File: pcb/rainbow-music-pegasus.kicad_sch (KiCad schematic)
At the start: 111 parts, among them J1 USB_B_Micro, J2 Conn_02x03_Odd_Even, J3 B2B-PH-K-S, Q1 DMG3415U, SW1 SW_SPDT, SW2 EVQQ2, U1 ESP32-C3-MINI-1, U2 OPA2322, U3 TLV75533PDBV, U4 MCP73831-2-OT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

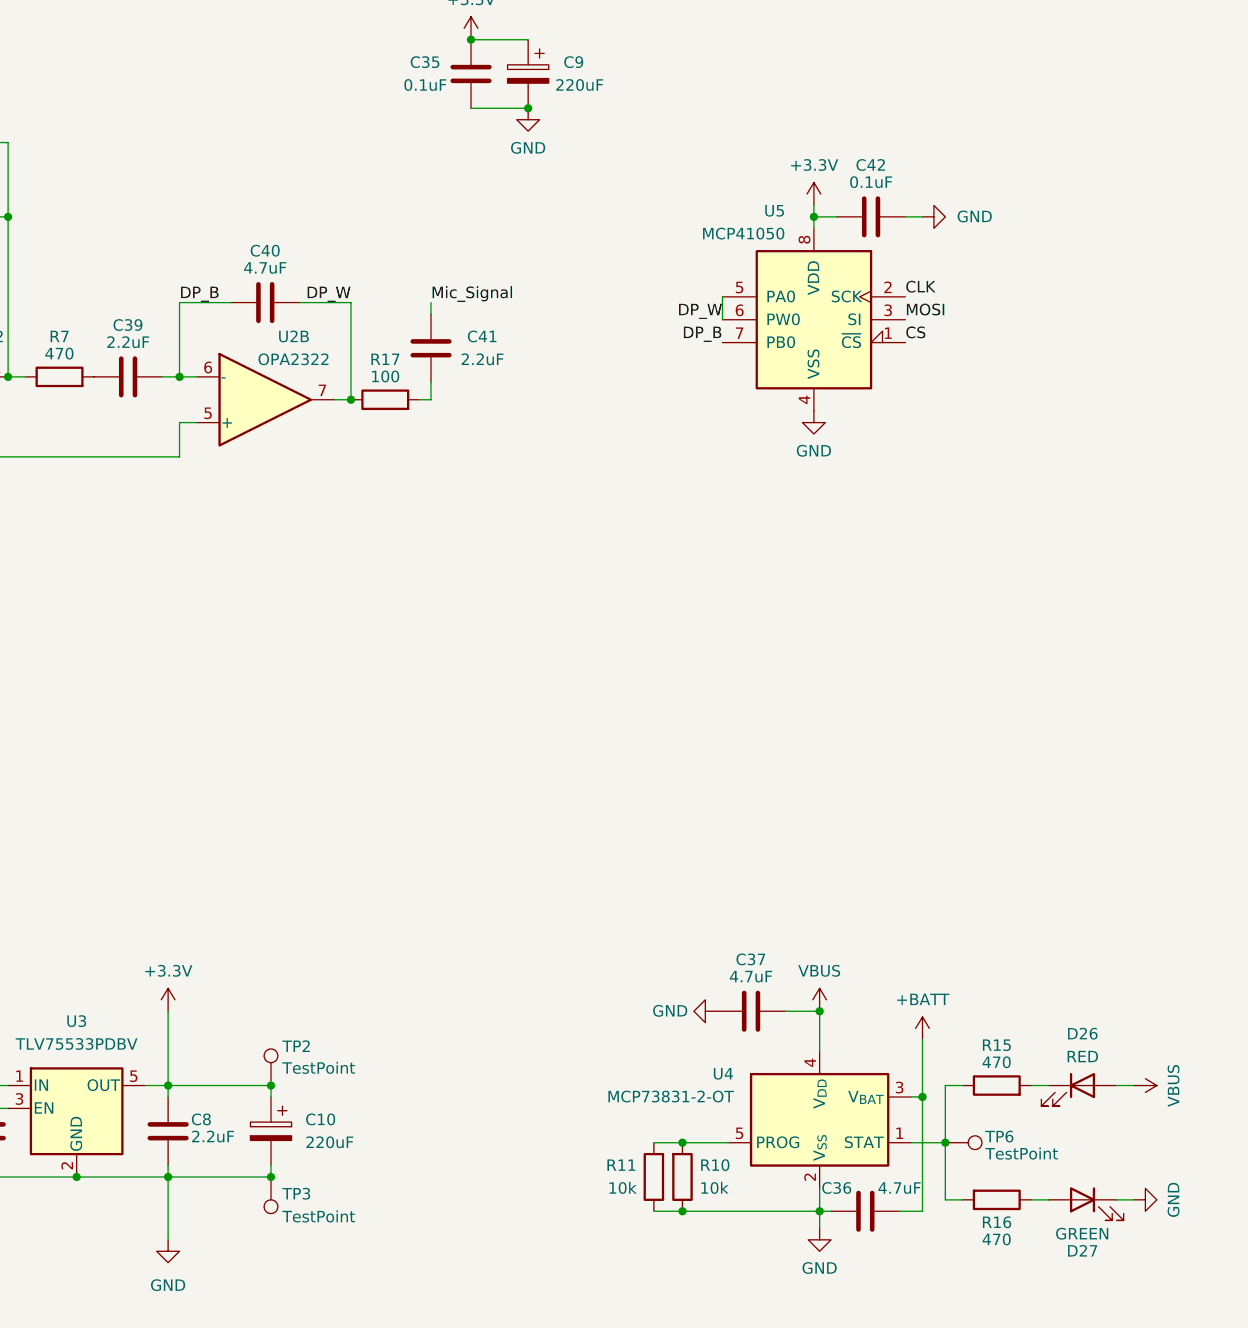
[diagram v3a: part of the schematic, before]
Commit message: Move TP6 to the DP_Wiper, add TP7 to DP_A and TP8 to MIC feed
Also fixed the size of all Touchpoints to allow for soldering thru-hole pins
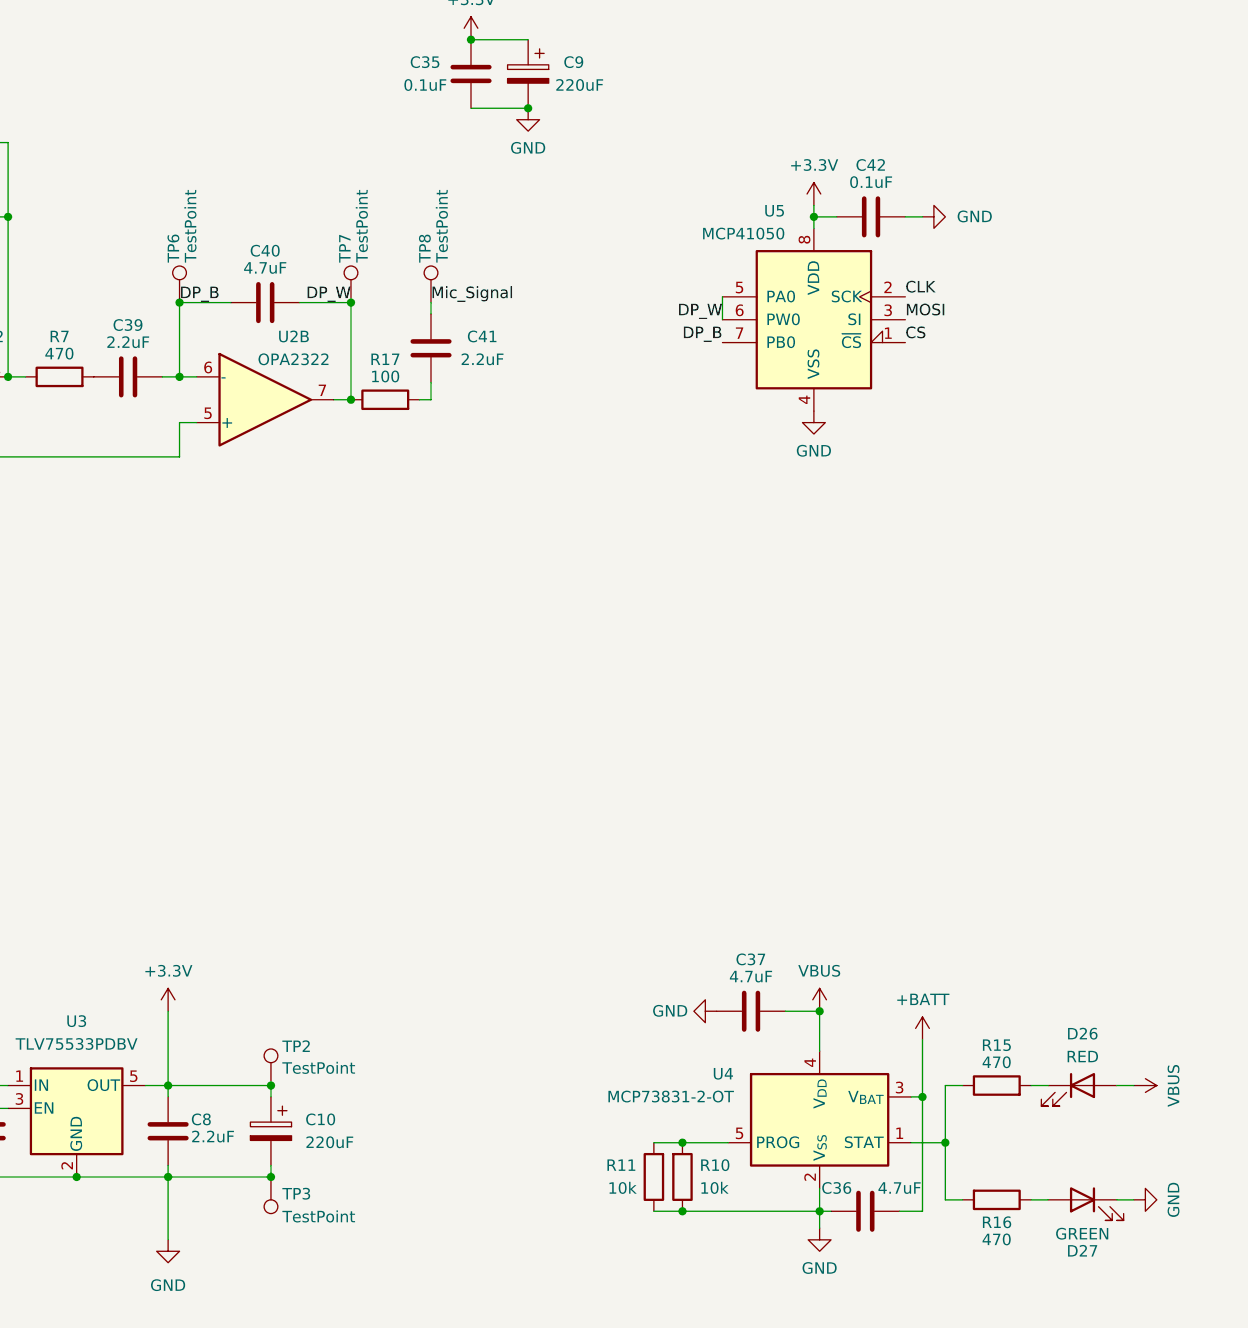
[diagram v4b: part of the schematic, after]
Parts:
- added TP7, TP8: TestPoint, TestPoint:TestPoint_THTPad_1.5x1.5mm_Drill0.7mm, symbol Connector:TestPoint
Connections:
- net DP_B: now also TP6.1
- net DP_W: now also TP7.1
- net Mic_Signal: now also TP8.1
- net at R15.1, R16.2, U4.1 (STAT): no longer TP6.1
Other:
- moved on the sheet: TP6
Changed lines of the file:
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@@
 	)
 	(junction
+		(at 133.35 62.23)
+		(diameter 0)
+		(color 0 0 0 0)
+	)
+	(junction
 		(at 170.18 163.195)
 		(diameter 0)
@@
 	)
 	(junction
+		(at 114.3 62.23)
+		(diameter 0)
+		(color 0 0 0 0)
+	)
+	(junction
 		(at 281.305 39.37)
 		(diameter 0)
@@
 	)
 	(symbol
+		(lib_id "Connector:TestPoint")
+		(at 133.35 62.23 0)
+		(mirror y)
+		(unit 1)
+		(exclude_from_sim no)
+		(in_bom no)
+		(on_board yes)
+		(dnp no)
+		(property "Reference" "TP7"
+			(at 132.715 57.785 90)
+			(effects
+				(font
+					(size 1.27 1.27)
+				)
+				(justify left)
+			)
+		)
+		(property "Value" "TestPoint"
+			(at 134.62 57.785 90)
+			(effects
+				(font
+					(size 1.27 1.27)
+				)
+				(justify left)
+			)
+		)
+		(property "Footprint" "TestPoint:TestPoint_THTPad_1.5x1.5mm_Drill0.7mm"
+			(at 128.27 62.23 0)
+			(effects
+				(font
+					(size 1.27 1.27)
+				)
+				(hide yes)
+			)
+		)
+		(property "Datasheet" "~"
+			(at 128.27 62.23 0)
+			(effects
+				(font
+					(size 1.27 1.27)
+				)
+				(hide yes)
+			)
+		)
+		(property "Description" ""
+			(at 133.35 62.23 0)
+			(effects
+				(font
+					(size 1.27 1.27)
+				)
+			)
+		)
+		(pin "1"
+		)
+		(instances
+			(project "rainbow-music-pegasus"
+				(path "/4cbaa20b-39f5-487e-a5d4-6b04539cf52b"
+					(reference "TP7")
+					(unit 1)
+				)
+			)
+		)
+	)
+	(symbol
 		(lib_id "power:+3.3V")
 		(at 269.24 230.505 0)
@@
 	(symbol
 		(lib_id "Connector:TestPoint")
-		(at 199.39 155.575 270)
-		(mirror x)
+		(at 114.3 62.23 0)
+		(mirror y)
 		(unit 1)
 		(exclude_from_sim no)
@@
 		(dnp no)
 		(property "Reference" "TP6"
-			(at 203.835 154.94 90)
+			(at 113.665 57.785 90)
 			(effects
 				(font
@@
 		)
 		(property "Value" "TestPoint"
-			(at 203.835 156.845 90)
+			(at 115.57 57.785 90)
 			(effects
 				(font
@@
 		)
 		(property "Footprint" "TestPoint:TestPoint_THTPad_1.5x1.5mm_Drill0.7mm"
-			(at 199.39 150.495 0)
+			(at 109.22 62.23 0)
 			(effects
 				(font
@@
 		)
 		(property "Datasheet" "~"
-			(at 199.39 150.495 0)
+			(at 109.22 62.23 0)
 			(effects
 				(font
@@
 		)
 		(property "Description" ""
-			(at 199.39 155.575 0)
+			(at 114.3 62.23 0)
 			(effects
 				(font
@@
 					(unit 1)
 				)
+			)
+		)
+	)
+	(symbol
+		(lib_id "Connector:TestPoint")
+		(at 142.24 62.23 0)
+		(mirror y)
+		(unit 1)
+		(exclude_from_sim no)
+		(in_bom no)
+		(on_board yes)
+		(dnp no)
+		(property "Reference" "TP8"
+			(at 141.605 57.785 90)
+			(effects
+				(font
+					(size 1.27 1.27)
+				)
+				(justify left)
+			)
+		)
+		(property "Value" "TestPoint"
+			(at 143.51 57.785 90)
+			(effects
+				(font
+					(size 1.27 1.27)
+				)
+				(justify left)
+			)
+		)
+		(property "Footprint" "TestPoint:TestPoint_THTPad_1.5x1.5mm_Drill0.7mm"
+			(at 137.16 62.23 0)
+			(effects
+				(font
+					(size 1.27 1.27)
+				)
+				(hide yes)
+			)
+		)
+		(property "Datasheet" "~"
+			(at 137.16 62.23 0)
+			(effects
+				(font
+					(size 1.27 1.27)
+				)
+				(hide yes)
+			)
+		)
+		(property "Description" ""
+			(at 142.24 62.23 0)
+			(effects
+				(font
+					(size 1.27 1.27)
+				)
+			)
+		)
+		(pin "1"
+		)
+		(instances
+			(project "rainbow-music-pegasus"
+				(path "/4cbaa20b-39f5-487e-a5d4-6b04539cf52b"
+					(reference "TP8")
+					(unit 1)
+				)
